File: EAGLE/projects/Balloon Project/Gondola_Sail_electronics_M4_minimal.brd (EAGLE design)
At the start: 114 x 100 mm, 34 parts

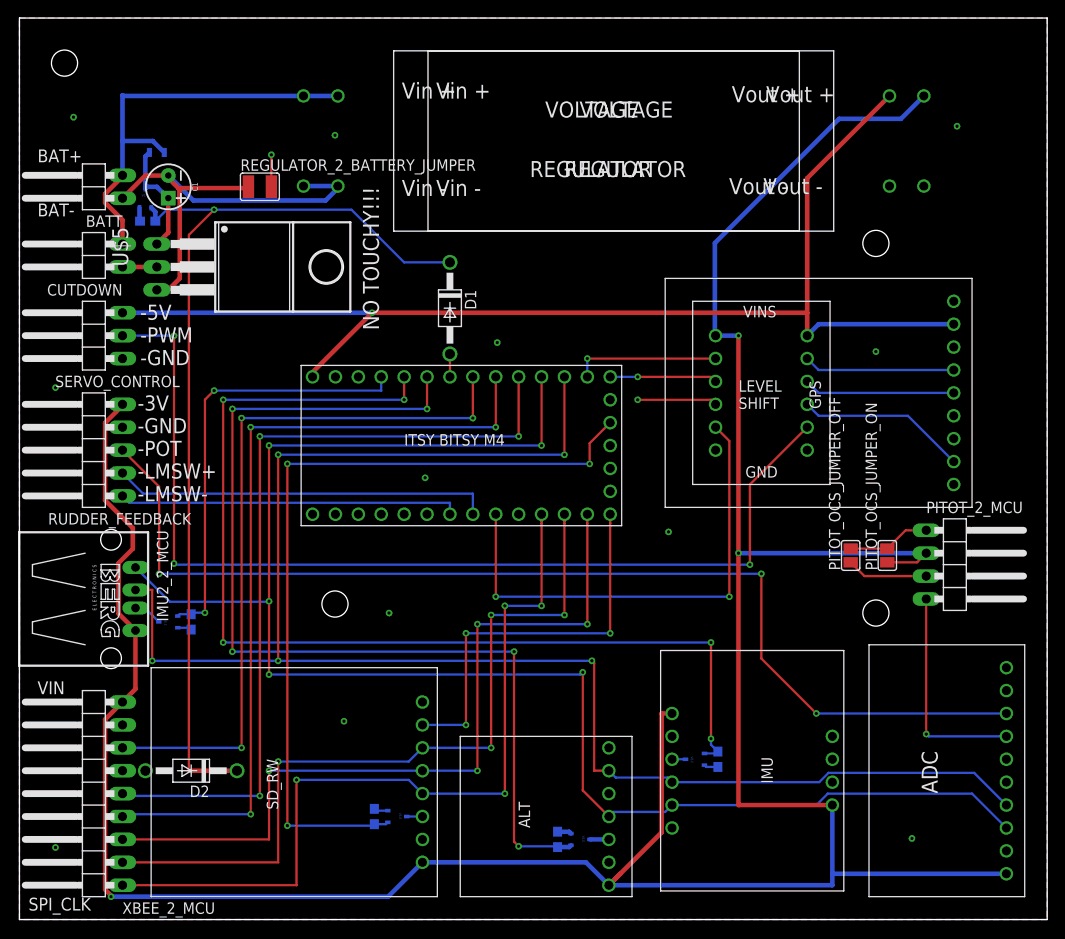
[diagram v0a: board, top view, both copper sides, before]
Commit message: optimized board layout - finished
-minimized vias
-optimized some routes
-added silkscreen to xbee
-ERC and DRC checks out for all boards
-ready for ordering
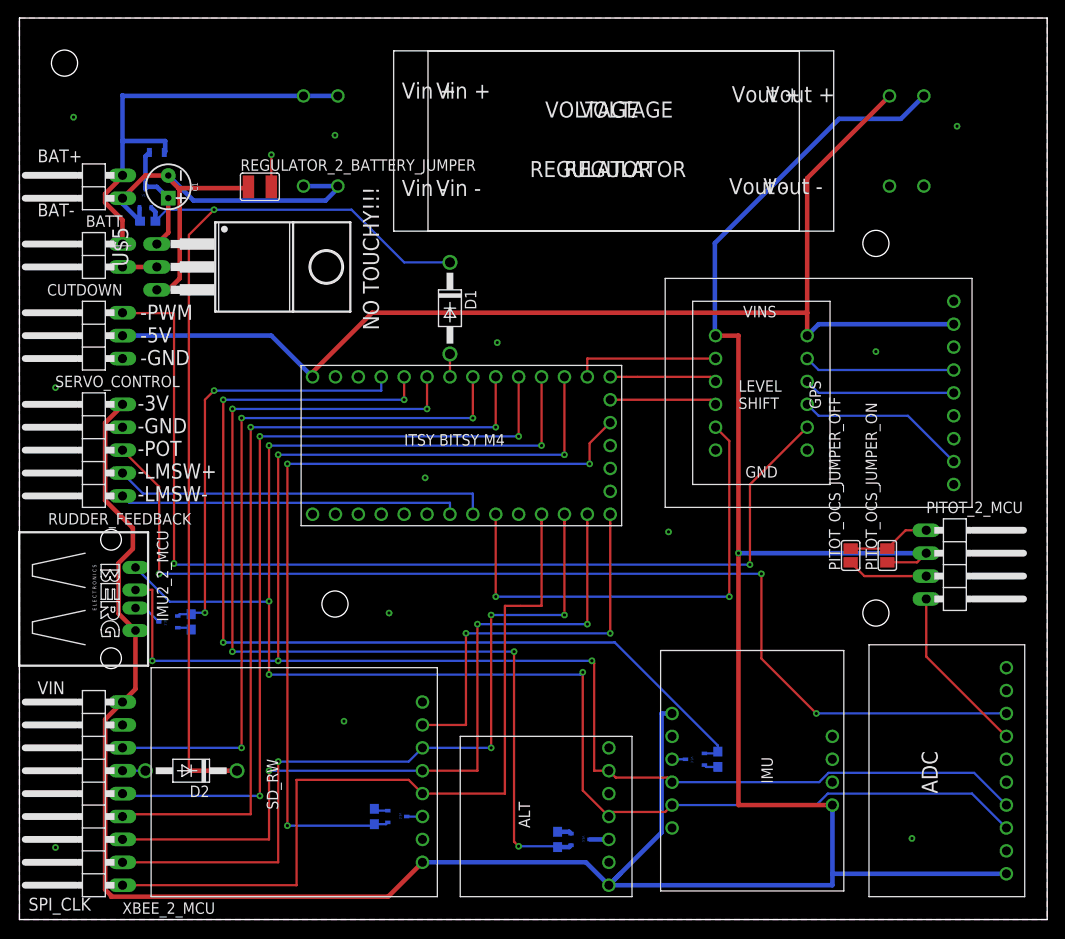
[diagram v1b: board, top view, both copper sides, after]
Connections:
- net 5V: now also SERVO_CONTROL.2; no longer SERVO_CONTROL.3
- net RUDDER_SERVO_PWM_5V: now also SERVO_CONTROL.3; no longer SERVO_CONTROL.2
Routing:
- net IMU1_PWR: track 117.6 -> 111.4 mm, vias 5 -> 3
- net PITOT_VAR: track 24.0 -> 18.9 mm, vias 1 -> 0
- net 5V: track 132.9 -> 128.2 mm, vias 1 -> 0
- net BATT_GND: track 55.5 -> 58.7 mm
- net GPS_EN_3V: track 8.85 -> 11.9 mm, vias 1 -> 0
- net XBEE_CUTDOWN: track 0.00 -> 2.54 mm
- net RUDDER_SERVO_PWM_5V: track 112.8 -> 115.3 mm, vias 3 -> 2
- net BATT_VIN: track 47.2 -> 48.1 mm
- net XBEE_ATTN: vias 3 -> 2
- net SPI_MISO: vias 4 -> 3
- net SPI_CLK: vias 4 -> 0
- net SD_CS: vias 3 -> 2
- net REG_GND: vias 1 -> 13
- net MCU_TX_3V: vias 1 -> 0
- net MCU_RX_3V: vias 1 -> 0
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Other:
- board text added: "-PWM -5V -GND"
- board text removed: "-5V -PWM -GND"
